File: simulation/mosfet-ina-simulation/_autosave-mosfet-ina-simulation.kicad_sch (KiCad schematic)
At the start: 25 parts, among them Q1 NMOS, U1 ${SIM.PARAMS}, U2 ${SIM.PARAMS}

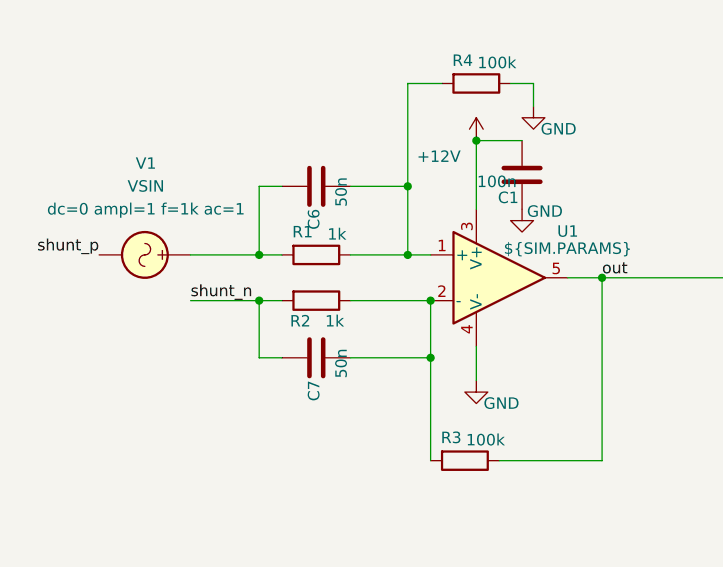
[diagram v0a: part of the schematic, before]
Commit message: upload C513170 to lib
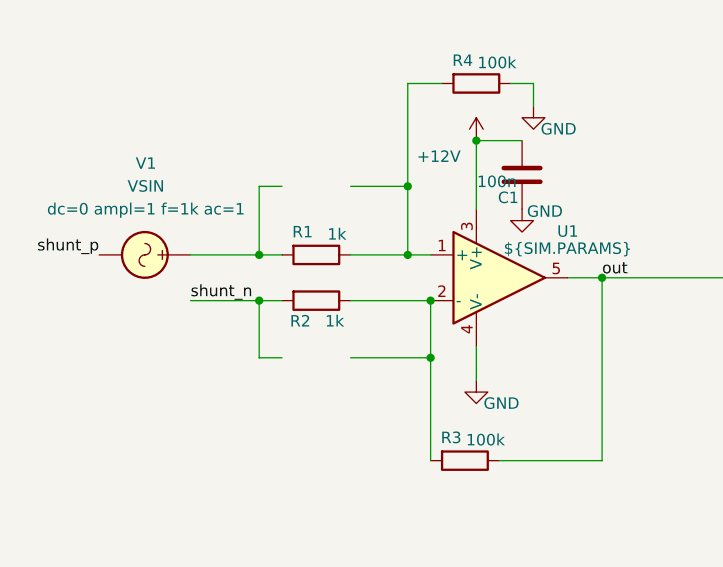
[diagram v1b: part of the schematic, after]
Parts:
- removed C6, C7: 50n, symbol Device:C
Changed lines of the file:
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@@
-	)
-	(symbol
-		(lib_id "Device:C")
-		(at 45.72 76.2 90)
-		(unit 1)
-		(exclude_from_sim no)
-		(in_bom yes)
-		(on_board yes)
-		(dnp no)
-		(property "Reference" "C7"
-			(at 45.466 81.026 0)
-			(effects
-				(font
-					(size 1.27 1.27)
-				)
-				(justify left)
-			)
-		)
-		(property "Value" "50n"
-			(at 48.514 78.486 0)
-			(effects
-				(font
-					(size 1.27 1.27)
-				)
-				(justify left)
-			)
-		)
-		(property "Footprint" ""
-			(at 49.53 75.2348 0)
-			(effects
-				(font
-					(size 1.27 1.27)
-				)
-				(hide yes)
-			)
-		)
-		(property "Datasheet" "~"
-			(at 45.72 76.2 0)
-			(effects
-				(font
-					(size 1.27 1.27)
-				)
-				(hide yes)
-			)
-		)
-		(property "Description" "Unpolarized capacitor"
-			(at 45.72 76.2 0)
-			(effects
-				(font
-					(size 1.27 1.27)
-				)
-				(hide yes)
-			)
-		)
-		(pin "1"
-		)
-		(pin "2"
-		)
-		(instances
-			(project "mosfet-ina-simulation"
-				(path "/c153c308-03e0-4d4b-a368-42bad221d52c"
-					(reference "C7")
-					(unit 1)
-				)
-			)
-		)
 	)
 	(symbol
@@
 					(unit 1)
 				)
-			)
-		)
-	)
-	(symbol
-		(lib_id "Device:C")
-		(at 45.72 57.15 90)
-		(unit 1)
-		(exclude_from_sim no)
-		(in_bom yes)
-		(on_board yes)
-		(dnp no)
-		(property "Reference" "C6"
-			(at 45.466 61.976 0)
-			(effects
-				(font
-					(size 1.27 1.27)
-				)
-				(justify left)
-			)
-		)
-		(property "Value" "50n"
-			(at 48.514 59.436 0)
-			(effects
-				(font
-					(size 1.27 1.27)
-				)
-				(justify left)
-			)
-		)
-		(property "Footprint" ""
-			(at 49.53 56.1848 0)
-			(effects
-				(font
-					(size 1.27 1.27)
-				)
-				(hide yes)
-			)
-		)
-		(property "Datasheet" "~"
-			(at 45.72 57.15 0)
-			(effects
-				(font
-					(size 1.27 1.27)
-				)
-				(hide yes)
-			)
-		)
-		(property "Description" "Unpolarized capacitor"
-			(at 45.72 57.15 0)
-			(effects
-				(font
-					(size 1.27 1.27)
-				)
-				(hide yes)
-			)
-		)
-		(pin "1"
-		)
-		(pin "2"
-		)
-		(instances
-			(project "mosfet-ina-simulation"
-				(path "/c153c308-03e0-4d4b-a368-42bad221d52c"
-					(reference "C6")
-					(unit 1)
-				)
